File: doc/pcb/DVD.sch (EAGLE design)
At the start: 33 parts, among them IC1 7805, IC2 74HC14N

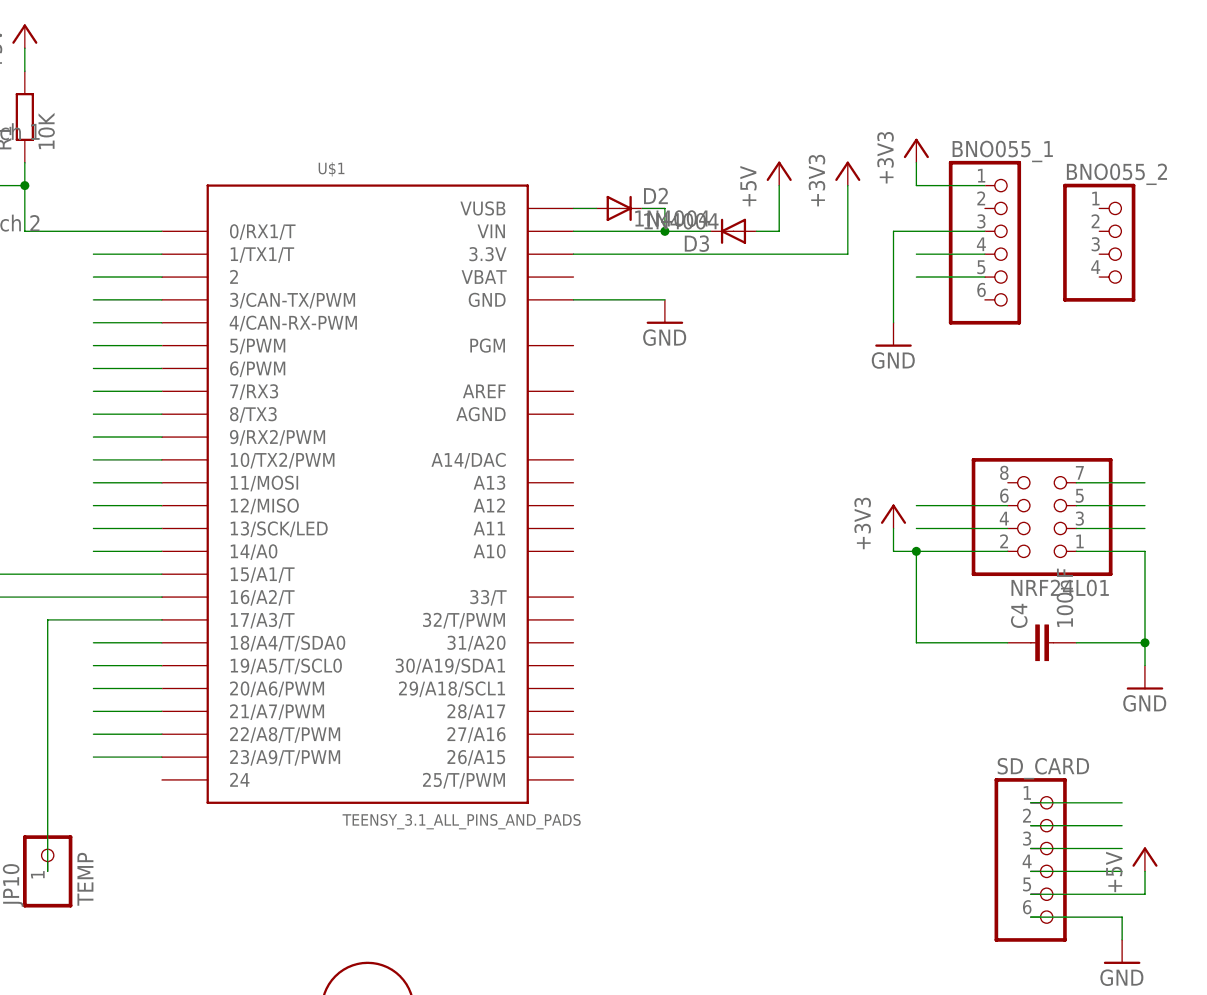
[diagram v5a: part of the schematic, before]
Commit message: Exchanged Teensy footprint PCB
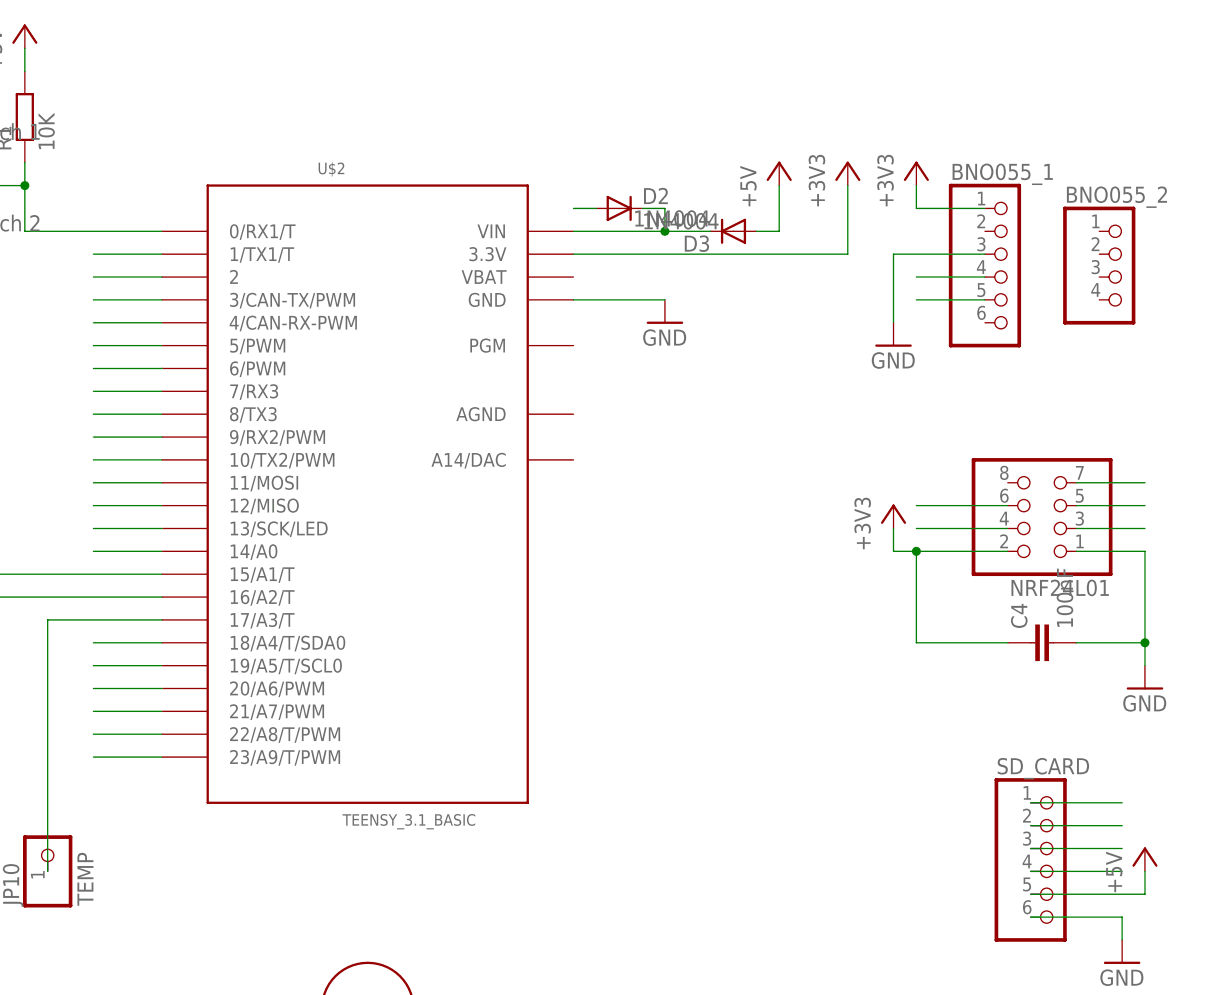
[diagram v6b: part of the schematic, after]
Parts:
- removed U$1: TEENSY_3.1_ALL_PINS_AND_PADS, Teensy_3_Series_Board_v1.0:TEENSY_3.1_ALL_PINS_AND_PADS
- added U$2: TEENSY_3.1_BASIC, Teensy_3_Series_Board_v1.0:TEENSY_3.1_BASIC
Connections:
- net +3V3: now also U$2.3.3V; no longer U$1.3.3V
- net CE: now also U$2.8/TX3; no longer U$1.8/TX3
- net CSN_RADIO: now also U$2.10/TX2/PWM; no longer U$1.10/TX2/PWM
- net CSN_SD: now also U$2.9/RX2/PWM; no longer U$1.9/RX2/PWM
- net D4_IR: now also U$2.4/CAN-RX-PWM; no longer U$1.4/CAN-RX-PWM
- net GND: now also U$2.GND; no longer U$1.GND
- net IN1: now also U$2.23/A9/T/PWM; no longer U$1.23/A9/T/PWM
- net IN2: now also U$2.22/A8/T/PWM; no longer U$1.22/A8/T/PWM
- net JP0: now also U$2.17/A3/T; no longer U$1.17/A3/T
- net MISO: now also U$2.12/MISO; no longer U$1.12/MISO
- net MOSI: now also U$2.11/MOSI; no longer U$1.11/MOSI
- net N$1: now also U$2.VIN; no longer U$1.VIN
- net N$10: now also U$2.15/A1/T; no longer U$1.15/A1/T
- net N$11: now also U$2.16/A2/T; no longer U$1.16/A2/T
- net N$18: now also U$2.0/RX1/T; no longer U$1.0/RX1/T
- net N$19: now also U$2.1/TX1/T; no longer U$1.1/TX1/T
- net N$20: now also U$2.2; no longer U$1.2
- net N$21: now also U$2.6/PWM; no longer U$1.6/PWM
- net N$22: now also U$2.7/RX3; no longer U$1.7/RX3
- net N$3: now also U$2.5/PWM; no longer U$1.5/PWM
- net N$4: no longer U$1.VUSB
- net N$9: now also U$2.13/SCK/LED; no longer U$1.13/SCK/LED
- net PWM: now also U$2.21/A7/PWM; no longer U$1.21/A7/PWM
- net SCK: now also U$2.14/A0; no longer U$1.14/A0
- net SCL: now also U$2.19/A5/T/SCL0; no longer U$1.19/A5/T/SCL0
- net SDA: now also U$2.18/A4/T/SDA0; no longer U$1.18/A4/T/SDA0
- net SPEED_SENSOR: now also U$2.3/CAN-TX/PWM; no longer U$1.3/CAN-TX/PWM
- net STBY: now also U$2.20/A6/PWM; no longer U$1.20/A6/PWM
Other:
- moved on the sheet: BNO055_1, BNO055_2

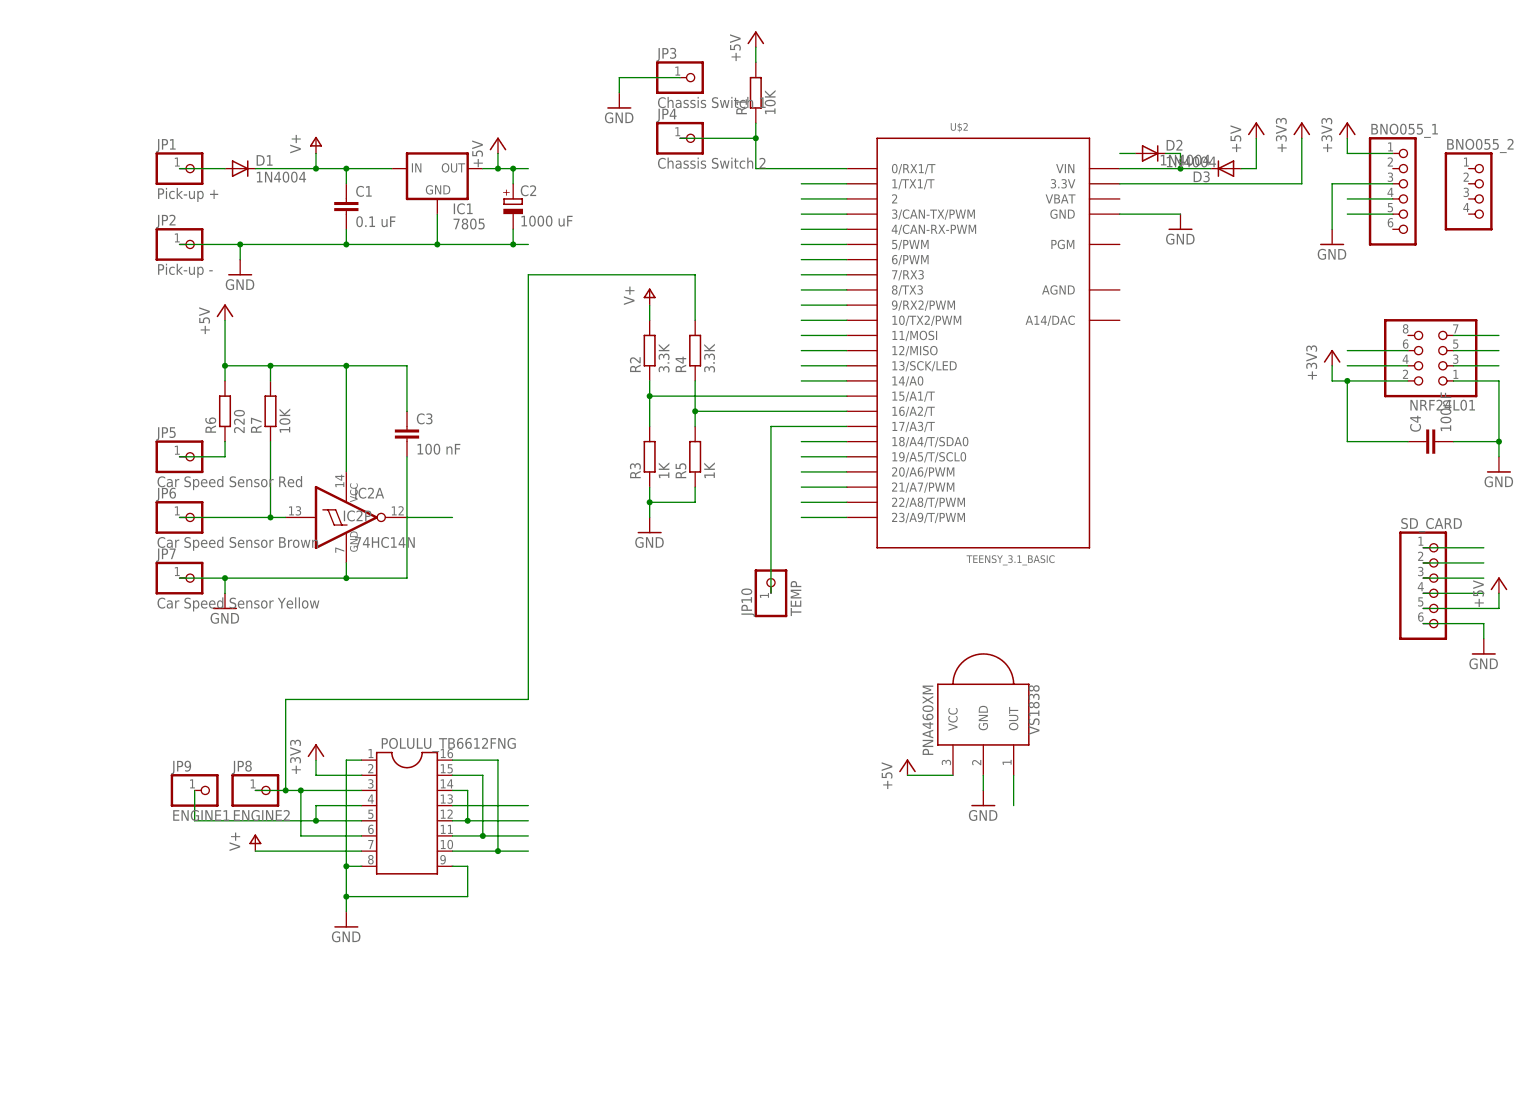
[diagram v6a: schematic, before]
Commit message: Fixed Pololu/BNO055/Teensy footprint
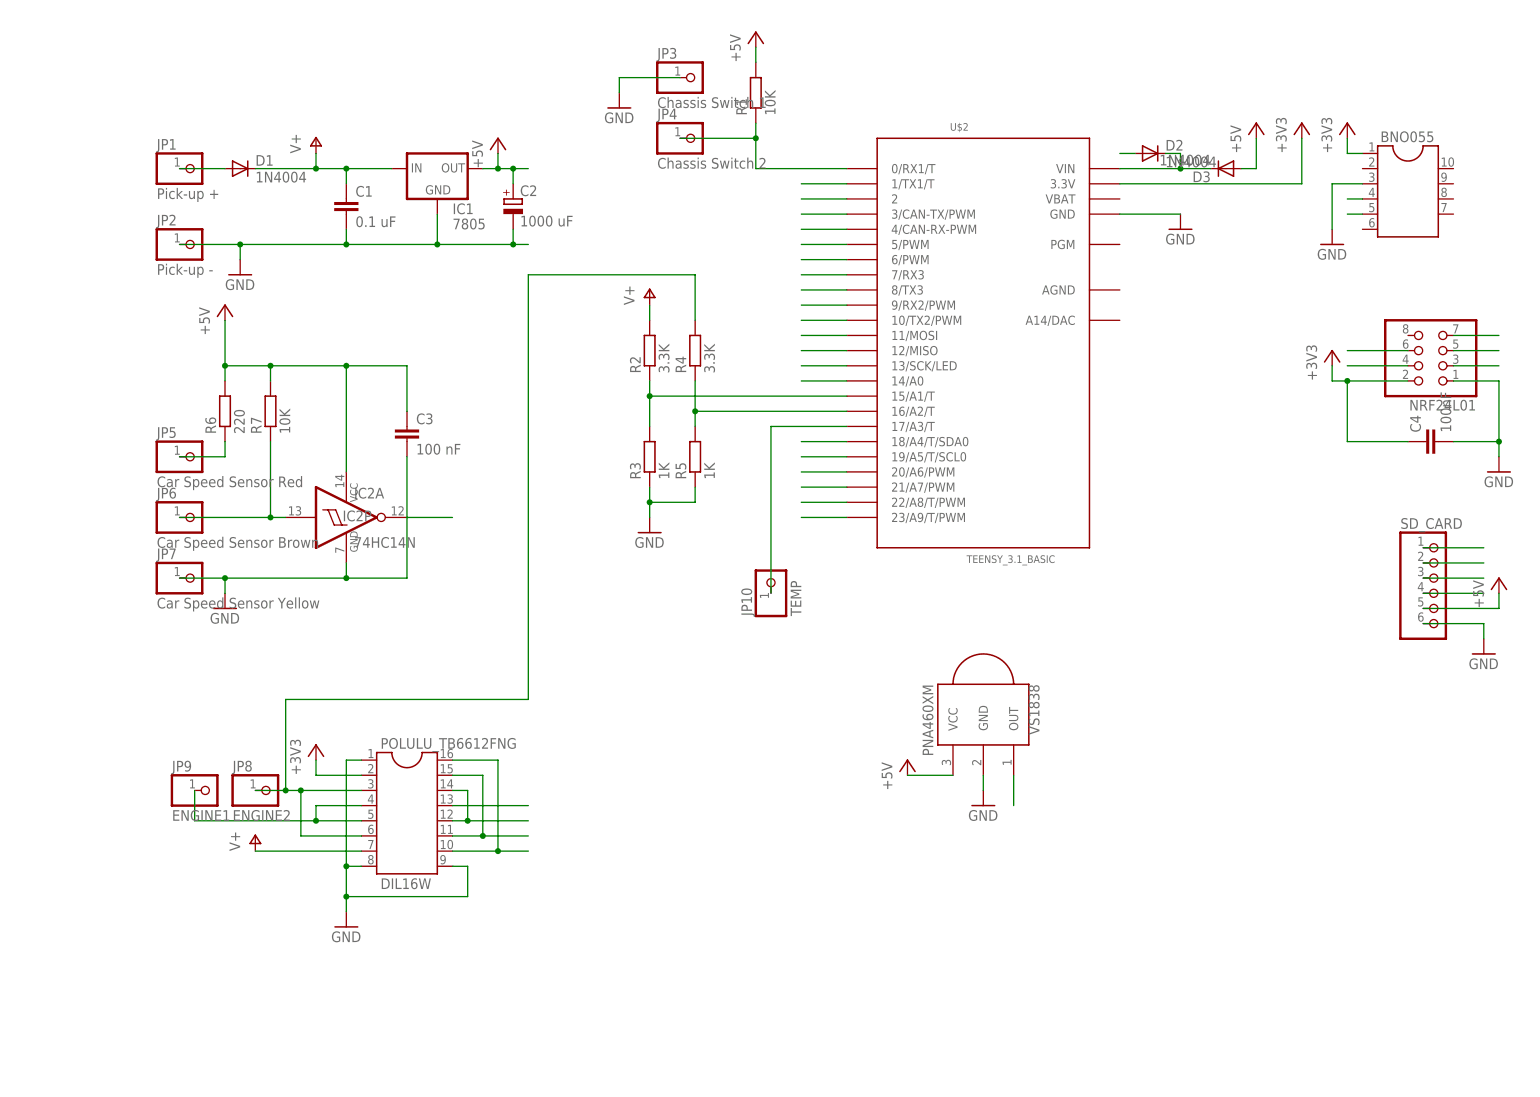
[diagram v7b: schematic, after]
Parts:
- removed BNO055_1: (no value), adafruit:PINHD-1X6
- removed BNO055_2: (no value), pinhead:PINHD-1X4
- added BNO055: (no value), ic-package_mod:DIL10-6-4
- POLULU_TB6612FNG: value (none) -> DIL16W; device ic-package:DIL16 -> ic-package_mod:DIL16W
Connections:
- net +3V3: now also BNO055.1; no longer BNO055_1.1
- net GND: now also BNO055.3; no longer BNO055_1.3
- net SCL: now also BNO055.5; no longer BNO055_1.5
- net SDA: now also BNO055.4; no longer BNO055_1.4
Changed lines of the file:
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@@
 <part name="GND11" library="supply1" deviceset="GND" device=""/>
 <part name="GND12" library="supply1" deviceset="GND" device=""/>
-<part name="BNO055_1" library="adafruit" deviceset="PINHD-1X6" device=""/>
-<part name="BNO055_2" library="pinhead" deviceset="PINHD-1X4" device=""/>
-<part name="POLULU_TB6612FNG" library="ic-package" deviceset="DIL16" device=""/>
 <part name="P+11" library="supply1" deviceset="V+" device=""/>
 <part name="C2" library="resistor" deviceset="CPOL-EU" device="P128-50" value="1000 uF"/>
@@
 <part name="D3" library="adafruit" deviceset="1N4004" device=""/>
 <part name="U$2" library="Teensy_3_Series_Board_v1.0" deviceset="TEENSY_3.1_BASIC" device=""/>
+<part name="POLULU_TB6612FNG" library="ic-package_mod" deviceset="DIL16W" device="" value="DIL16W"/>
+<part name="BNO055" library="ic-package_mod" deviceset="DIL10-6-4" device=""/>
 </parts>
 <sheets>
@@
 <instance part="GND11" gate="1" x="10.16" y="12.7"/>
 <instance part="GND12" gate="1" x="175.26" y="127"/>
-<instance part="BNO055_1" gate="A" x="187.96" y="134.62"/>
-<instance part="BNO055_2" gate="A" x="200.66" y="134.62"/>
-<instance part="POLULU_TB6612FNG" gate="G$1" x="20.32" y="33.02"/>
 <instance part="P+11" gate="1" x="-5.08" y="27.94"/>
 <instance part="IC2" gate="P" x="10.16" y="81.28"/>
@@
 <instance part="D3" gate="1" x="157.48" y="139.7" rot="R180"/>
 <instance part="U$2" gate="G$1" x="116.84" y="111.76"/>
+<instance part="POLULU_TB6612FNG" gate="G$1" x="20.32" y="33.02"/>
+<instance part="BNO055" gate="G$1" x="187.96" y="137.16" rot="MR0"/>
 </instances>
 <busses>
@@
 </segment>
 <segment>
-<pinref part="POLULU_TB6612FNG" gate="G$1" pin="7"/>
 <wire x1="12.7" y1="25.4" x2="-5.08" y2="25.4" width="0.1524" layer="91"/>
 <pinref part="P+11" gate="1" pin="V+"/>
+<pinref part="POLULU_TB6612FNG" gate="G$1" pin="7"/>
 </segment>
 <segment>
@@
 </segment>
 <segment>
-<pinref part="BNO055_1" gate="A" pin="3"/>
-<wire x1="185.42" y1="137.16" x2="175.26" y2="137.16" width="0.1524" layer="91"/>
+<wire x1="180.34" y1="137.16" x2="175.26" y2="137.16" width="0.1524" layer="91"/>
 <wire x1="175.26" y1="137.16" x2="175.26" y2="129.54" width="0.1524" layer="91"/>
 <pinref part="GND12" gate="1" pin="GND"/>
-</segment>
-<segment>
-<pinref part="POLULU_TB6612FNG" gate="G$1" pin="1"/>
+<pinref part="BNO055" gate="G$1" pin="3"/>
+</segment>
+<segment>
 <wire x1="12.7" y1="40.64" x2="10.16" y2="40.64" width="0.1524" layer="91"/>
 <wire x1="10.16" y1="40.64" x2="10.16" y2="22.86" width="0.1524" layer="91"/>
 <wire x1="10.16" y1="15.24" x2="10.16" y2="17.78" width="0.1524" layer="91"/>
-<pinref part="POLULU_TB6612FNG" gate="G$1" pin="8"/>
 <wire x1="12.7" y1="22.86" x2="10.16" y2="22.86" width="0.1524" layer="91"/>
 <wire x1="10.16" y1="22.86" x2="10.16" y2="17.78" width="0.1524" layer="91"/>
 <wire x1="10.16" y1="17.78" x2="30.48" y2="17.78" width="0.1524" layer="91"/>
 <wire x1="30.48" y1="17.78" x2="30.48" y2="22.86" width="0.1524" layer="91"/>
-<pinref part="POLULU_TB6612FNG" gate="G$1" pin="9"/>
 <wire x1="30.48" y1="22.86" x2="27.94" y2="22.86" width="0.1524" layer="91"/>
 <junction x="10.16" y="22.86"/>
 <junction x="10.16" y="17.78"/>
 <pinref part="GND11" gate="1" pin="GND"/>
+<pinref part="POLULU_TB6612FNG" gate="G$1" pin="1"/>
+<pinref part="POLULU_TB6612FNG" gate="G$1" pin="8"/>
+<pinref part="POLULU_TB6612FNG" gate="G$1" pin="9"/>
 </segment>
 </net>
@@
 </segment>
 <segment>
+<wire x1="27.94" y1="33.02" x2="40.64" y2="33.02" width="0.1524" layer="91"/>
 <pinref part="POLULU_TB6612FNG" gate="G$1" pin="13"/>
-<wire x1="27.94" y1="33.02" x2="40.64" y2="33.02" width="0.1524" layer="91"/>
 </segment>
 </net>
@@
 </segment>
 <segment>
-<pinref part="BNO055_1" gate="A" pin="1"/>
-<wire x1="185.42" y1="142.24" x2="177.8" y2="142.24" width="0.1524" layer="91"/>
+<wire x1="180.34" y1="142.24" x2="177.8" y2="142.24" width="0.1524" layer="91"/>
 <wire x1="177.8" y1="142.24" x2="177.8" y2="144.78" width="0.1524" layer="91"/>
 <pinref part="+3V4" gate="G$1" pin="+3V3"/>
-</segment>
-<segment>
-<pinref part="POLULU_TB6612FNG" gate="G$1" pin="2"/>
+<pinref part="BNO055" gate="G$1" pin="1"/>
+</segment>
+<segment>
 <wire x1="12.7" y1="38.1" x2="5.08" y2="38.1" width="0.1524" layer="91"/>
 <pinref part="+3V3" gate="G$1" pin="+3V3"/>
 <wire x1="5.08" y1="38.1" x2="5.08" y2="40.64" width="0.1524" layer="91"/>
+<pinref part="POLULU_TB6612FNG" gate="G$1" pin="2"/>
 </segment>
 </net>
@@
 <net name="SDA" class="0">
 <segment>
-<pinref part="BNO055_1" gate="A" pin="4"/>
-<wire x1="185.42" y1="134.62" x2="177.8" y2="134.62" width="0.1524" layer="91"/>
+<wire x1="180.34" y1="134.62" x2="177.8" y2="134.62" width="0.1524" layer="91"/>
+<pinref part="BNO055" gate="G$1" pin="4"/>
 </segment>
 <segment>
@@
 <net name="SCL" class="0">
 <segment>
-<pinref part="BNO055_1" gate="A" pin="5"/>
-<wire x1="185.42" y1="132.08" x2="177.8" y2="132.08" width="0.1524" layer="91"/>
+<wire x1="180.34" y1="132.08" x2="177.8" y2="132.08" width="0.1524" layer="91"/>
+<pinref part="BNO055" gate="G$1" pin="5"/>
 </segment>
 <segment>
@@
 <net name="JP8" class="0">
 <segment>
-<pinref part="POLULU_TB6612FNG" gate="G$1" pin="6"/>
 <wire x1="12.7" y1="27.94" x2="2.54" y2="27.94" width="0.1524" layer="91"/>
 <wire x1="2.54" y1="27.94" x2="2.54" y2="35.56" width="0.1524" layer="91"/>
-<pinref part="POLULU_TB6612FNG" gate="G$1" pin="3"/>
 <pinref part="JP8" gate="G$1" pin="1"/>
 <wire x1="12.7" y1="35.56" x2="2.54" y2="35.56" width="0.1524" layer="91"/>
@@
 <wire x1="0" y1="50.8" x2="0" y2="35.56" width="0.1524" layer="91"/>
 <junction x="0" y="35.56"/>
+<pinref part="POLULU_TB6612FNG" gate="G$1" pin="3"/>
+<pinref part="POLULU_TB6612FNG" gate="G$1" pin="6"/>
 </segment>
 </net>
 <net name="ENGINE1" class="0">
 <segment>
-<pinref part="POLULU_TB6612FNG" gate="G$1" pin="4"/>
 <wire x1="12.7" y1="33.02" x2="5.08" y2="33.02" width="0.1524" layer="91"/>
 <wire x1="5.08" y1="33.02" x2="5.08" y2="30.48" width="0.1524" layer="91"/>
-<pinref part="POLULU_TB6612FNG" gate="G$1" pin="5"/>
 <wire x1="12.7" y1="30.48" x2="5.08" y2="30.48" width="0.1524" layer="91"/>
 <pinref part="JP9" gate="G$1" pin="1"/>
@@
 <wire x1="-15.24" y1="30.48" x2="-15.24" y2="35.56" width="0.1524" layer="91"/>
 <junction x="5.08" y="30.48"/>
+<pinref part="POLULU_TB6612FNG" gate="G$1" pin="4"/>
+<pinref part="POLULU_TB6612FNG" gate="G$1" pin="5"/>
 </segment>
 </net>
 <net name="IN1" class="0">
 <segment>
-<pinref part="POLULU_TB6612FNG" gate="G$1" pin="14"/>
 <wire x1="27.94" y1="35.56" x2="30.48" y2="35.56" width="0.1524" layer="91"/>
 <wire x1="30.48" y1="35.56" x2="30.48" y2="30.48" width="0.1524" layer="91"/>
-<pinref part="POLULU_TB6612FNG" gate="G$1" pin="12"/>
 <wire x1="27.94" y1="30.48" x2="30.48" y2="30.48" width="0.1524" layer="91"/>
 <junction x="30.48" y="30.48"/>
 <wire x1="30.48" y1="30.48" x2="40.64" y2="30.48" width="0.1524" layer="91"/>
+<pinref part="POLULU_TB6612FNG" gate="G$1" pin="12"/>
+<pinref part="POLULU_TB6612FNG" gate="G$1" pin="14"/>
 </segment>
 <segment>
@@
 <net name="IN2" class="0">
 <segment>
-<pinref part="POLULU_TB6612FNG" gate="G$1" pin="15"/>
 <wire x1="27.94" y1="38.1" x2="33.02" y2="38.1" width="0.1524" layer="91"/>
 <wire x1="33.02" y1="38.1" x2="33.02" y2="27.94" width="0.1524" layer="91"/>
-<pinref part="POLULU_TB6612FNG" gate="G$1" pin="11"/>
 <wire x1="27.94" y1="27.94" x2="33.02" y2="27.94" width="0.1524" layer="91"/>
 <junction x="33.02" y="27.94"/>
 <wire x1="33.02" y1="27.94" x2="40.64" y2="27.94" width="0.1524" layer="91"/>
+<pinref part="POLULU_TB6612FNG" gate="G$1" pin="11"/>
+<pinref part="POLULU_TB6612FNG" gate="G$1" pin="15"/>
 </segment>
 <segment>
@@
 <net name="PWM" class="0">
 <segment>
-<pinref part="POLULU_TB6612FNG" gate="G$1" pin="16"/>
 <wire x1="27.94" y1="40.64" x2="35.56" y2="40.64" width="0.1524" layer="91"/>
 <wire x1="35.56" y1="40.64" x2="35.56" y2="25.4" width="0.1524" layer="91"/>
-<pinref part="POLULU_TB6612FNG" gate="G$1" pin="10"/>
 <wire x1="27.94" y1="25.4" x2="35.56" y2="25.4" width="0.1524" layer="91"/>
 <junction x="35.56" y="25.4"/>
 <wire x1="35.56" y1="25.4" x2="40.64" y2="25.4" width="0.1524" layer="91"/>
-</segment>
-<segment>
+<pinref part="POLULU_TB6612FNG" gate="G$1" pin="10"/>
+<pinref part="POLULU_TB6612FNG" gate="G$1" pin="16"/>
+</segment>
+<segment>
